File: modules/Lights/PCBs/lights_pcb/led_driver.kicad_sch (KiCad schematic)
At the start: 18 parts, among them J5 Conn_01x04_Pin, J6 Conn_01x03_Pin, J8 Barrel_Jack, Q1 RFP30N06LE, Q2 RFP30N06LE, Q3 RFP30N06LE, Q7 2N7000, Q8 2N7000, SW2 SW_SPDT, U3 ISO6740, U4 LM4040BIZ-5

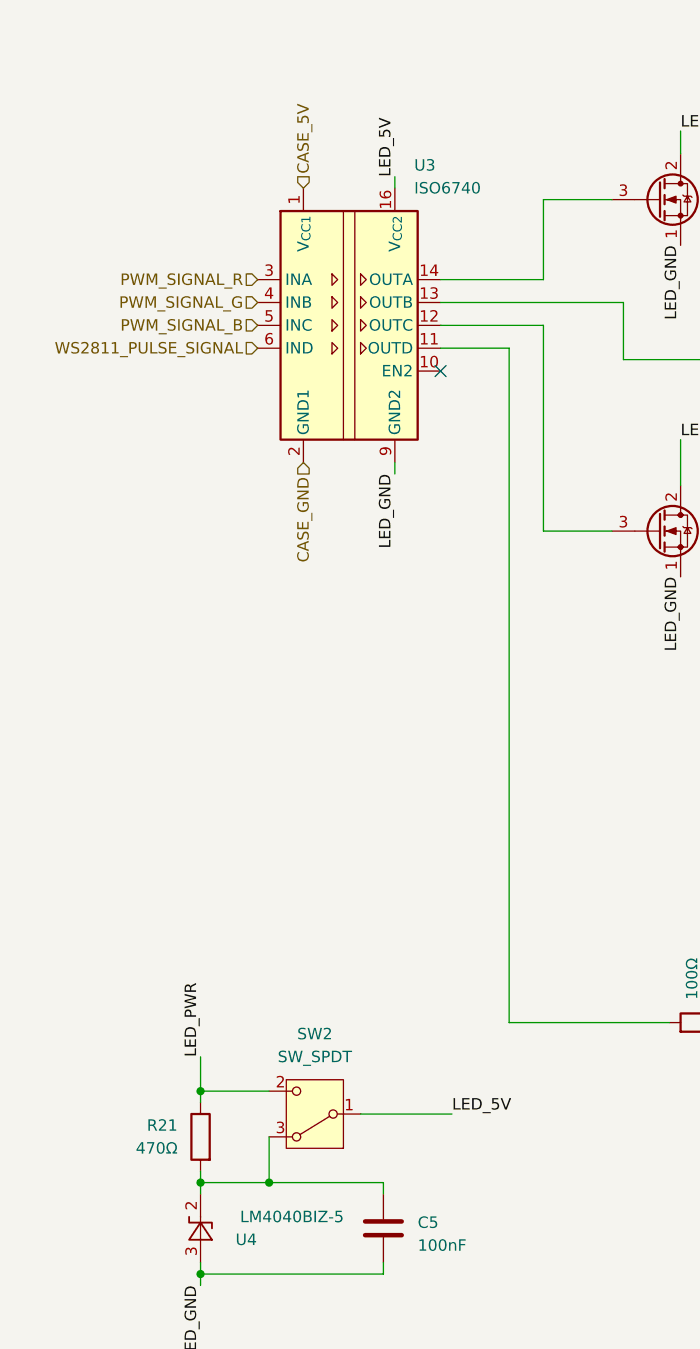
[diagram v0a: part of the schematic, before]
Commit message: Switch lights to external 3.3V power supply instead of using rpi pico
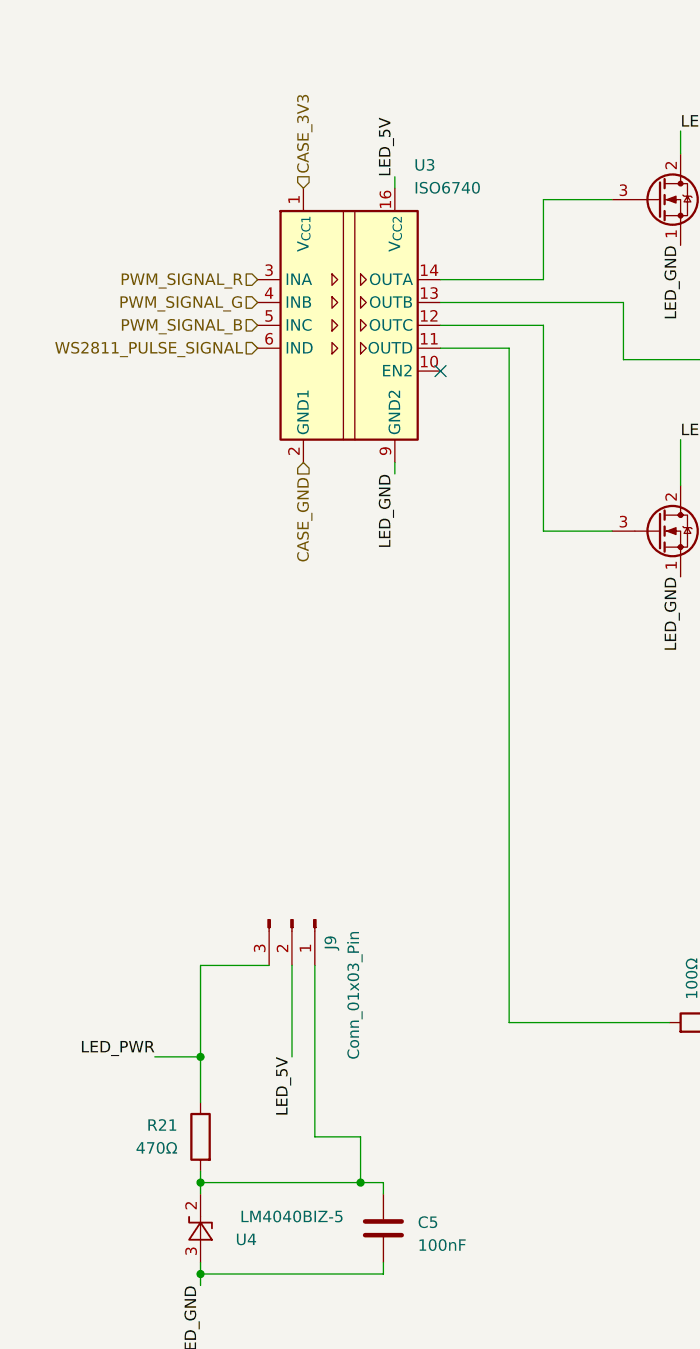
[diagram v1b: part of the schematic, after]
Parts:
- removed SW2: SW_SPDT, Button_Switch_THT:SW_Slide-03_Wuerth-WS-SLTV_10x2.5x6.4_P2.54mm, symbol Switch:SW_SPDT_312
- added J9: Conn_01x03_Pin, Connector_PinSocket_2.54mm:PinSocket_1x03_P2.54mm_Vertical, symbol Connector:Conn_01x03_Pin
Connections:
- net LED_5V: now also J9.2 (Pin_2)
- net LED_PWR: now also J9.3 (Pin_3)
- net at C5.1, R21.2, U4.2 (K): now also J9.1 (Pin_1)
- net CASE_5V renamed CASE_3V3
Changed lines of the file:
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@@
-	)
-	(junction
-		(at 52.07 165.1)
-		(diameter 0)
-		(color 0 0 0 0)
 	)
 	(junction
@@
 	)
 	(junction
-		(at 44.45 154.94)
+		(at 44.45 151.13)
 		(diameter 0)
 		(color 0 0 0 0)
@@
 	)
 	(junction
+		(at 62.23 165.1)
+		(diameter 0)
+		(color 0 0 0 0)
+	)
+	(junction
 		(at 242.57 120.65)
 		(diameter 0)
@@
 	(wire
 		(pts
+			(xy 39.37 151.13) (xy 44.45 151.13)
+		)
+		(stroke
+			(width 0)
+			(type default)
+		)
+	)
+	(wire
+		(pts
 			(xy 82.55 64.77) (xy 82.55 55.88)
 		)
@@
 	(wire
 		(pts
+			(xy 44.45 151.13) (xy 44.45 156.21)
+		)
+		(stroke
+			(width 0)
+			(type default)
+		)
+	)
+	(wire
+		(pts
 			(xy 140.97 132.08) (xy 140.97 129.54)
 		)
@@
 	(wire
 		(pts
-			(xy 62.23 157.48) (xy 72.39 157.48)
+			(xy 54.61 140.97) (xy 54.61 151.13)
+		)
+		(stroke
+			(width 0)
+			(type default)
+		)
+	)
+	(wire
+		(pts
+			(xy 57.15 140.97) (xy 57.15 160.02)
 		)
 		(stroke
@@
 	(wire
 		(pts
-			(xy 44.45 154.94) (xy 52.07 154.94)
-		)
-		(stroke
-			(width 0)
-			(type default)
-		)
-	)
-	(wire
-		(pts
-			(xy 64.77 165.1) (xy 52.07 165.1)
+			(xy 44.45 140.97) (xy 52.07 140.97)
+		)
+		(stroke
+			(width 0)
+			(type default)
+		)
+	)
+	(wire
+		(pts
+			(xy 64.77 165.1) (xy 62.23 165.1)
 		)
 		(stroke
@@
 	(wire
 		(pts
-			(xy 44.45 151.13) (xy 44.45 154.94)
-		)
-		(stroke
-			(width 0)
-			(type default)
-		)
-	)
-	(wire
-		(pts
 			(xy 110.49 73.66) (xy 91.44 73.66)
 		)
@@
 	(wire
 		(pts
-			(xy 52.07 165.1) (xy 44.45 165.1)
+			(xy 44.45 165.1) (xy 62.23 165.1)
 		)
 		(stroke
@@
 	(wire
 		(pts
+			(xy 57.15 160.02) (xy 62.23 160.02)
+		)
+		(stroke
+			(width 0)
+			(type default)
+		)
+	)
+	(wire
+		(pts
 			(xy 252.73 118.11) (xy 252.73 120.65)
 		)
@@
 	(wire
 		(pts
-			(xy 44.45 154.94) (xy 44.45 156.21)
-		)
-		(stroke
-			(width 0)
-			(type default)
-		)
-	)
-	(wire
-		(pts
-			(xy 52.07 160.02) (xy 52.07 165.1)
+			(xy 44.45 140.97) (xy 44.45 151.13)
+		)
+		(stroke
+			(width 0)
+			(type default)
+		)
+	)
+	(wire
+		(pts
+			(xy 62.23 160.02) (xy 62.23 165.1)
 		)
 		(stroke
@@
 	)
 	(label "LED_PWR"
-		(at 44.45 151.13 90)
-		(effects
-			(font
-				(size 1.27 1.27)
-			)
-			(justify left bottom)
+		(at 39.37 151.13 180)
+		(effects
+			(font
+				(size 1.27 1.27)
+			)
+			(justify right bottom)
 		)
 	)
@@
 	)
 	(label "LED_5V"
-		(at 72.39 157.48 0)
-		(effects
-			(font
-				(size 1.27 1.27)
-			)
-			(justify left bottom)
+		(at 54.61 151.13 270)
+		(effects
+			(font
+				(size 1.27 1.27)
+			)
+			(justify right bottom)
 		)
 	)
@@
 		)
 	)
-	(hierarchical_label "CASE_5V"
+	(hierarchical_label "CASE_3V3"
 		(shape input)
 		(at 55.88 54.61 90)
@@
 		(length 2.54)
 		(shape round)
-		(at 64.77 157.48 0)
+		(at 54.61 149.86 90)
 		(fields_autoplaced yes)
 		(effects
@@
 		)
 		(property "Netclass" "Power"
-			(at 65.4685 154.94 0)
+			(at 52.07 149.1615 90)
 			(effects
 				(font
@@
 		)
 		(property "Component Class" ""
-			(at -73.66 21.59 0)
+			(at -83.82 13.97 0)
 			(effects
 				(font
@@
 	)
 	(symbol
-		(lib_id "Switch:SW_SPDT_312")
-		(at 57.15 157.48 180)
+		(lib_id "Connector:Conn_01x03_Pin")
+		(at 54.61 135.89 270)
 		(unit 1)
 		(exclude_from_sim no)
@@
 		(on_board yes)
 		(dnp no)
-		(property "Reference" "SW2"
-			(at 57.15 148.59 0)
-			(effects
-				(font
-					(size 1.27 1.27)
-				)
-			)
-		)
-		(property "Value" "SW_SPDT"
-			(at 57.15 151.13 0)
-			(effects
-				(font
-					(size 1.27 1.27)
-				)
-			)
-		)
-		(property "Footprint" "Button_Switch_THT:SW_Slide-03_Wuerth-WS-SLTV_10x2.5x6.4_P2.54mm"
-			(at 57.15 147.32 0)
+		(property "Reference" "J9"
+			(at 58.928 138.43 0)
+			(effects
+				(font
+					(size 1.27 1.27)
+				)
+			)
+		)
+		(property "Value" "Conn_01x03_Pin"
+			(at 61.468 144.272 0)
+			(effects
+				(font
+					(size 1.27 1.27)
+				)
+			)
+		)
+		(property "Footprint" "Connector_PinSocket_2.54mm:PinSocket_1x03_P2.54mm_Vertical"
+			(at 54.61 135.89 0)
 			(effects
 				(font
@@
 		)
 		(property "Datasheet" "~"
-			(at 57.15 149.86 0)
+			(at 54.61 135.89 0)
 			(effects
 				(font
@@
 			)
 		)
-		(property "Description" "Switch, single pole double throw"
-			(at 57.15 157.48 0)
+		(property "Description" "Generic connector, single row, 01x03, script generated"
+			(at 54.61 135.89 0)
 			(effects
 				(font
@@
 			)
 		)
+		(pin "2"
+		)
+		(pin "3"
+		)
 		(pin "1"
-		)
-		(pin "3"
-		)
-		(pin "2"
 		)
 		(instances
 			(project ""
 				(path "/bf0b830d-6ea8-4ffe-b350-63f7ac69529d/fb67f68a-97d2-4622-a1dc-f7d875308de8/d5458d77-62c7-4a68-894a-9d5a4d1294f9"
-					(reference "SW2")
+					(reference "J9")
 					(unit 1)
 				)
